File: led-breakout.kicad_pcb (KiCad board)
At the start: 2 copper layers, 31 parts, among them J1 LED_STRIP, J10 LED3, J11 LED4, J12 LED5, J13 LED6, J14 LED7, J15 LED8, J2 Raspberry_Pi_2_3, J3 POWER, J4 I2C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

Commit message: hopefully last revision
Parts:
- added F1: Fuse, Fuse_Holders_and_Fuses:Fuse_SMD1206_HandSoldering, F.Cu at (141.6, 133.3)
- added F2: Fuse, Fuse_Holders_and_Fuses:Fuse_SMD1206_HandSoldering, F.Cu at (143.5, 146.1)
- added F3: Fuse, Fuse_Holders_and_Fuses:Fuse_SMD1206_HandSoldering, F.Cu at (143.5, 150.5)
- moved J3 1.91 mm to (156.2, 146.7)
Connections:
- J1 pad 2: Net-(J1-Pad2) -> Net-(F3-Pad2)
- J1 pad 3: Net-(J1-Pad3) -> Net-(F2-Pad2)
- J1 pad 4: Net-(J1-Pad4) -> Net-(F1-Pad2)
- Q1 pad 3: Net-(J1-Pad4) -> Net-(F1-Pad1)
- Q2 pad 3: Net-(J1-Pad3) -> Net-(F2-Pad1)
- Q3 pad 3: Net-(J1-Pad2) -> Net-(F3-Pad1)
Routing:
- net Net-(J1-Pad4): track 18.4 -> 0.00 mm
- net Net-(J1-Pad3): track 12.3 -> 0.00 mm
- net Net-(J1-Pad2): track 11.7 -> 0.00 mm
- net Net-(F1-Pad2): track 0.00 -> 11.0 mm
- net GNDREF: track 139.6 -> 149.1 mm
- net Net-(J2-Pad19): track 17.6 -> 25.2 mm
- net Net-(F2-Pad1): track 0.00 -> 5.81 mm
- net Net-(J2-Pad11): track 101.4 -> 96.1 mm
- net Net-(J2-Pad40): track 82.2 -> 86.5 mm, vias 0 -> 2
- net Net-(F3-Pad2): track 0.00 -> 3.89 mm
- net Net-(J2-Pad24): track 17.6 -> 21.4 mm
- net Net-(F3-Pad1): track 0.00 -> 3.75 mm
- net Net-(F1-Pad1): track 0.00 -> 3.48 mm
- net Net-(F2-Pad2): track 0.00 -> 2.99 mm
- net Net-(J2-Pad35): track 80.4 -> 78.7 mm
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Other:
- net class Default: clearance 0.2 -> 0.15; trace_width 0.25 -> 0.2
- net class LED-power: clearance 0.1 -> 0.2; trace_width 0.2 -> 0.25
- net class hi-voltage: clearance 0.7 -> 0.4; trace_width 1 -> 0.5
- rule trace_clearance: 0.2 -> 0.15
- board text added: "BOTTOM"
- board text added: "LED STRIP: MAX 1 A PER CHANNEL"
- board text added: "TOP"
- board text removed: "MAX: 1A"

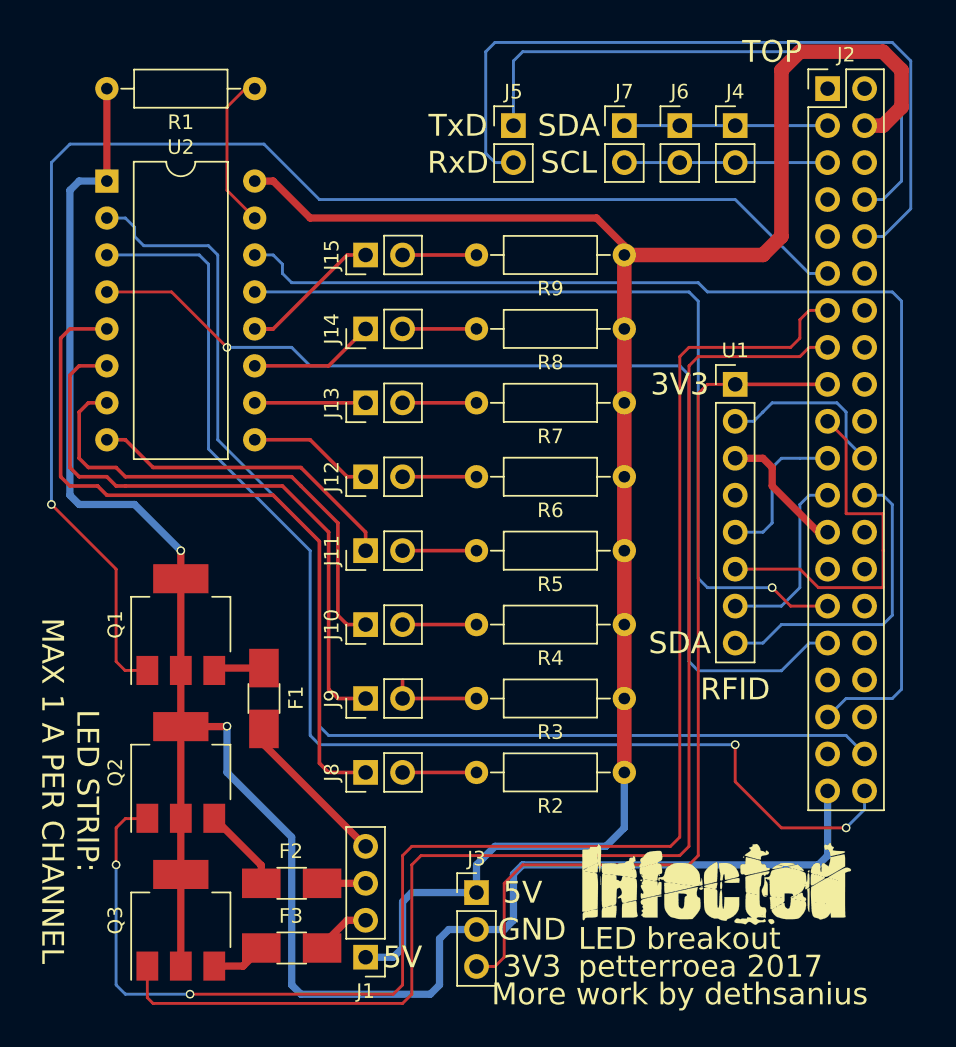
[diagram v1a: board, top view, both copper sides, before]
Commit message: new revision of v3: now with filling
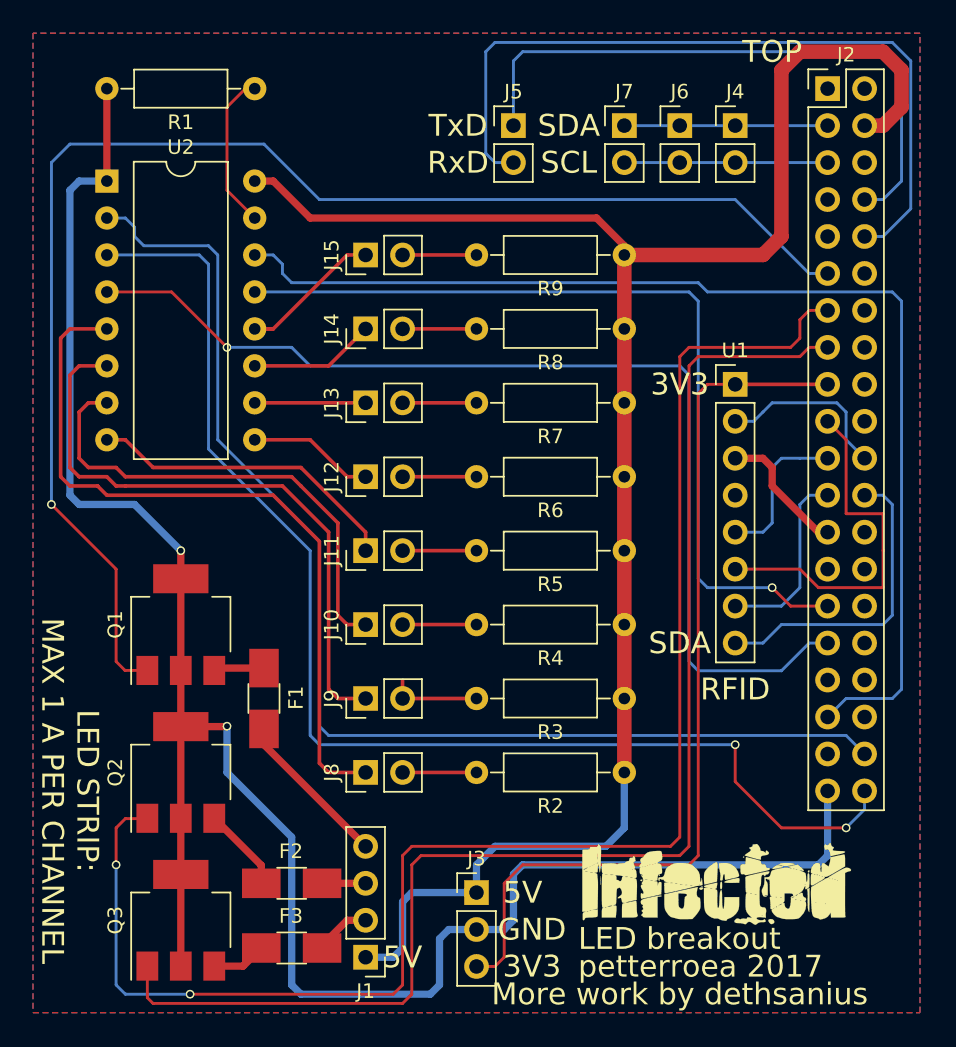
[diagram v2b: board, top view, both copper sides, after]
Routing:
- added copper zone on B.Cu, net GNDREF
- added copper zone on F.Cu, net GNDREF
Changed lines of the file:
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@@
   (general
     (links 69)
-    (no_connects 2)
+    (no_connects 0)
     (area 125.645 87.7 188.533811 155.37)
     (thickness 1.6)
@@
   (segment (start 184.785 120.015) (end 184.785 127.635) (width 0.2) (layer B.Cu) (net 23))
   (segment (start 184.15 119.38) (end 184.785 120.015) (width 0.2) (layer B.Cu) (net 23))
-  (segment (start 140.97 105.41) (end 170.815 105.41) (width 0.2) (layer B.Cu) (net 27) (status 400000))
-  (segment (start 177.8 127) (end 180.34 127) (width 0.2) (layer F.Cu) (net 27) (status 800000))
+  (segment (start 140.97 105.41) (end 170.815 105.41) (width 0.2) (layer B.Cu) (net 27))
+  (segment (start 177.8 127) (end 180.34 127) (width 0.2) (layer F.Cu) (net 27))
   (segment (start 176.53 125.73) (end 177.8 127) (width 0.2) (layer F.Cu) (net 27))
   (via (at 176.53 125.73) (size 0.6) (drill 0.4) (layers F.Cu B.Cu) (net 27))
@@
   (segment (start 177.165 131.445) (end 171.45 131.445) (width 0.2) (layer B.Cu) (net 29))
   (segment (start 179.07 129.54) (end 177.165 131.445) (width 0.2) (layer B.Cu) (net 29))
-  (segment (start 180.34 134.62) (end 181.61 133.35) (width 0.2) (layer B.Cu) (net 33) (status 400000))
-  (segment (start 142.24 102.87) (end 140.97 102.87) (width 0.2) (layer B.Cu) (net 33) (status 800000))
+  (segment (start 180.34 134.62) (end 181.61 133.35) (width 0.2) (layer B.Cu) (net 33))
+  (segment (start 142.24 102.87) (end 140.97 102.87) (width 0.2) (layer B.Cu) (net 33))
   (segment (start 142.875 103.505) (end 142.24 102.87) (width 0.2) (layer B.Cu) (net 33))
   (segment (start 142.875 104.14) (end 142.875 103.505) (width 0.2) (layer B.Cu) (net 33))
@@
   (segment (start 145.6 150.31) (end 147.32 148.59) (width 0.5) (layer F.Cu) (net 62))
   (segment (start 147.32 148.59) (end 148.59 148.59) (width 0.5) (layer F.Cu) (net 62))
+  (zone (net 6) (net_name GNDREF) (layer F.Cu) (hatch edge 0.508)
+    (connect_pads (clearance 0.508))
+    (min_thickness 0.254)
+    (fill yes (arc_segments 16) (thermal_gap 0.508) (thermal_bridge_width 0.508))
+    (polygon
+      (pts
+        (xy 186.69 154.94) (xy 186.69 87.63) (xy 125.73 87.63) (xy 125.73 154.94)
+      )
+    )
+  )
+  (zone (net 6) (net_name GNDREF) (layer B.Cu) (hatch edge 0.508)
+    (connect_pads (clearance 0.508))
+    (min_thickness 0.254)
+    (fill yes (arc_segments 16) (thermal_gap 0.508) (thermal_bridge_width 0.508))
+    (polygon
+      (pts
+        (xy 186.69 154.94) (xy 186.69 87.63) (xy 125.73 87.63) (xy 125.73 154.94)
+      )
+    )
+  )
 )

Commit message: led breakout v4
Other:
- board text added: "Assembled by:"
- board text added: "Serial:"
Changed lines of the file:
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@@
     (links 69)
     (no_connects 0)
-    (area 125.645 87.7 188.533811 155.37)
+    (area 125.645 87.63 188.533811 155.37)
     (thickness 1.6)
-    (drawings 19)
+    (drawings 21)
     (tracks 316)
     (zones 0)
@@
   (page A4)
   (layers
-    (0 F.Cu signal)
+    (0 F.Cu signal hide)
     (31 B.Cu signal)
     (32 B.Adhes user)
@@
     (35 F.Paste user)
     (36 B.SilkS user)
-    (37 F.SilkS user)
+    (37 F.SilkS user hide)
     (38 B.Mask user)
     (39 F.Mask user)
@@
     (visible_elements FFFFFF7F)
     (pcbplotparams
-      (layerselection 0x00030_80000001)
+      (layerselection 0x000f0_80000001)
       (usegerberextensions false)
       (excludeedgelayer true)
@@
       (drillshape 0)
       (scaleselection 1)
-      (outputdirectory manufacture_v3/))
+      (outputdirectory manufacture_v4/))
   )
   (net 0 "")
@@
       (net 62 "Net-(F3-Pad2)"))
   )
-  (gr_text BOTTOM (at 174.625 88.9) (layer B.SilkS)
+  (gr_text Serial: (at 139.7 135.89) (layer B.SilkS)
+    (effects (font (size 1.5 1.5) (thickness 0.3)) (justify mirror))
+  )
+  (gr_text "Assembled by:" (at 134.62 123.19) (layer B.SilkS)
+    (effects (font (size 1.5 1.5) (thickness 0.3)) (justify mirror))
+  )
+  (gr_text BOTTOM (at 151.13 89.535) (layer B.SilkS)
     (effects (font (size 1.5 1.5) (thickness 0.3)) (justify mirror))
   )
@@
       )
     )
+  )
+  (zone (net 0) (net_name "") (layer B.SilkS) (hatch edge 0.508)
+    (connect_pads (clearance 0.508))
+    (min_thickness 0.254)
+    (fill yes (arc_segments 16) (thermal_gap 0.508) (thermal_bridge_width 0.508))
+    (polygon
+      (pts
+        (xy 126.365 125.095) (xy 142.875 125.095) (xy 142.875 133.985) (xy 126.365 133.985)
+      )
+    )
+  )
+  (zone (net 0) (net_name "") (layer B.SilkS) (hatch edge 0.508)
+    (connect_pads (clearance 0.508))
+    (min_thickness 0.254)
+    (fill yes (arc_segments 16) (thermal_gap 0.508) (thermal_bridge_width 0.508))
+    (polygon
+      (pts
+        (xy 126.365 137.795) (xy 142.875 137.795) (xy 142.875 144.78) (xy 126.365 144.78)
+      )
+    )

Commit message: Edge router path
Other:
- board outline added: 61 x 67.3 mm
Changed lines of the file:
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@@
     (links 69)
     (no_connects 0)
-    (area 125.645 87.63 188.533811 155.37)
+    (area 125.645 87.579999 188.533811 155.37)
     (thickness 1.6)
-    (drawings 21)
+    (drawings 25)
     (tracks 316)
     (zones 0)
@@
     (visible_elements FFFFFF7F)
     (pcbplotparams
-      (layerselection 0x000f0_80000001)
+      (layerselection 0x010f0_80000001)
       (usegerberextensions false)
       (excludeedgelayer true)
@@
       (net 62 "Net-(F3-Pad2)"))
   )
+  (gr_line (start 125.73 154.94) (end 125.73 87.63) (angle 90) (layer Edge.Cuts) (width 0.1))
+  (gr_line (start 186.69 154.94) (end 125.73 154.94) (angle 90) (layer Edge.Cuts) (width 0.1))
+  (gr_line (start 186.69 87.63) (end 186.69 154.94) (angle 90) (layer Edge.Cuts) (width 0.1))
+  (gr_line (start 125.73 87.63) (end 186.69 87.63) (angle 90) (layer Edge.Cuts) (width 0.1))
   (gr_text Serial: (at 139.7 135.89) (layer B.SilkS)
     (effects (font (size 1.5 1.5) (thickness 0.3)) (justify mirror))
